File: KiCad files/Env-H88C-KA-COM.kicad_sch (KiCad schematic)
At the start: 218 parts, among them J1 TSA343G00-250J2, U1 SOT-23-5 5.5V 3.3V 500mA, U2 RP2040

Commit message: general progress
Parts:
- removed D1: 1N4002W, Diode_SMD:D_SOD-123, symbol Device:D_Schottky
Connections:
- net D+ is gone; now on net USB_D+: D18.3 (I/O2), USB1.6 (DP1), USB1.8 (DP2)
- net D- is gone; now on net USB_D-: D18.2 (I/O1), USB1.5 (DN2), USB1.7 (DN1)
- net VSYS is gone; now on net VBUS: F1.2
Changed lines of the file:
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@@
   (junction (at 342.9 43.18) (diameter 0) (color 0 0 0 0)
   )
-  (junction (at 39.37 256.54) (diameter 0) (color 0 0 0 0)
-  )
   (junction (at 241.3 43.18) (diameter 0) (color 0 0 0 0)
   )
@@
     (stroke (width 0) (type default) (color 0 0 0 0))
   )
-  (wire (pts (xy 39.37 256.54) (xy 39.37 257.81))
-    (stroke (width 0) (type default) (color 0 0 0 0))
-  )
   (wire (pts (xy 266.7 93.98) (xy 292.1 93.98))
     (stroke (width 0) (type default) (color 0 0 0 0))
@@
     (stroke (width 0) (type default) (color 0 0 0 0))
   )
-  (wire (pts (xy 30.48 256.54) (xy 39.37 256.54))
-    (stroke (width 0) (type default) (color 0 0 0 0))
-  )
   (wire (pts (xy 347.98 82.55) (xy 354.33 82.55))
     (stroke (width 0) (type default) (color 0 0 0 0))
@@
     (stroke (width 0) (type default) (color 0 0 0 0))
   )
-  (wire (pts (xy 39.37 256.54) (xy 41.91 256.54))
+  (wire (pts (xy 30.48 256.54) (xy 49.53 256.54))
     (stroke (width 0) (type default) (color 0 0 0 0))
   )
@@
     (effects (font (size 1.27 1.27)) (justify right bottom))
   )
+  (label "USB_D+" (at 88.9 219.71 0)
+    (effects (font (size 1.27 1.27)) (justify left bottom))
+  )
   (label "GPIO3" (at 299.72 307.34 180)
     (effects (font (size 1.27 1.27)) (justify right bottom))
@@
     (effects (font (size 1.27 1.27)) (justify left bottom))
   )
+  (label "USB_D-" (at 88.9 191.77 0)
+    (effects (font (size 1.27 1.27)) (justify left bottom))
+  )
   (label "GPIO19" (at 299.72 347.98 180)
     (effects (font (size 1.27 1.27)) (justify right bottom))
@@
     )
   )
-  (global_label "D-" (shape input) (at 88.9 191.77 0) (fields_autoplaced)
-    (effects (font (size 1.27 1.27)) (justify left))
-    (property "Intersheet References" "${INTERSHEET_REFS}" (id 0) (at 94.1555 191.6906 0)
-      (effects (font (size 1.27 1.27)) (justify left) hide)
-    )
-  )
   (global_label "lock2" (shape input) (at 551.18 336.55 180) (fields_autoplaced)
     (effects (font (size 1.27 1.27)) (justify right))
@@
     )
   )
-  (global_label "D+" (shape input) (at 88.9 219.71 0) (fields_autoplaced)
-    (effects (font (size 1.27 1.27)) (justify left))
-    (property "Intersheet References" "${INTERSHEET_REFS}" (id 0) (at 94.1555 219.6306 0)
-      (effects (font (size 1.27 1.27)) (justify left) hide)
-    )
-  )
   (global_label "VSYS" (shape input) (at 55.88 256.54 180) (fields_autoplaced)
     (effects (font (size 0.508 0.508)) (justify right))
@@
     (pin "2")
   )
-  (symbol (lib_id "Device:D_Schottky") (at 45.72 256.54 180) (unit 1)
-    (in_bom yes) (on_board yes)
-    (property "Reference" "D1" (id 0) (at 45.72 251.0282 0))
-    (property "Value" "1N4002W" (id 1) (at 45.72 253.3396 0))
-    (property "Footprint" "Diode_SMD:D_SOD-123" (id 2) (at 45.72 256.54 0)
-      (effects (font (size 1.27 1.27)) hide)
-    )
-    (property "Datasheet" "" (id 3) (at 45.72 256.54 0)
-      (effects (font (size 1.27 1.27)) hide)
-    )
-    (property "LCSC" " " (id 4) (at 45.72 256.54 0)
-      (effects (font (size 1.27 1.27)) hide)
-    )
-    (pin "1")
-    (pin "2")
-  )
   (symbol (lib_id "MX_Alps_Hybrid:MX-NoLED") (at 191.77 33.02 0) (unit 1)
     (in_bom yes) (on_board yes)
@@
       (reference "CBP1") (unit 1) (value "10uf 0402") (footprint "Capacitor_SMD:C_0402_1005Metric")
     )
-    (path "/8ad5387f-3794-4c4f-b55f-a5df62f92cbd"
-      (reference "D1") (unit 1) (value "1N4002W") (footprint "Diode_SMD:D_SOD-123")
-    )
     (path "/4b543e59-5223-4ac5-868a-176e1cc9c1ca"

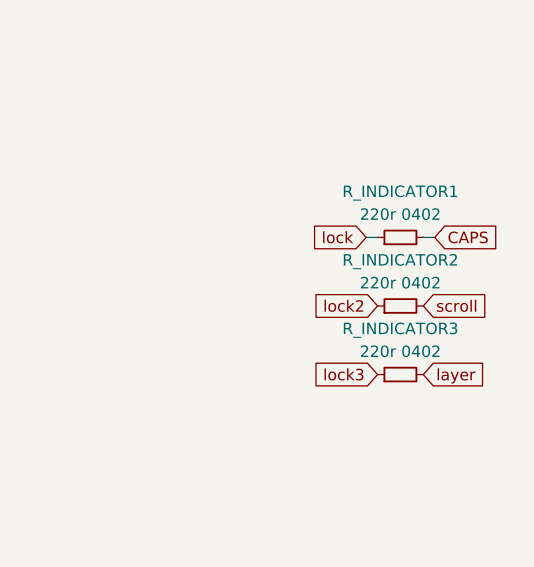
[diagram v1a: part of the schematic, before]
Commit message: slight rework to F12 TKL
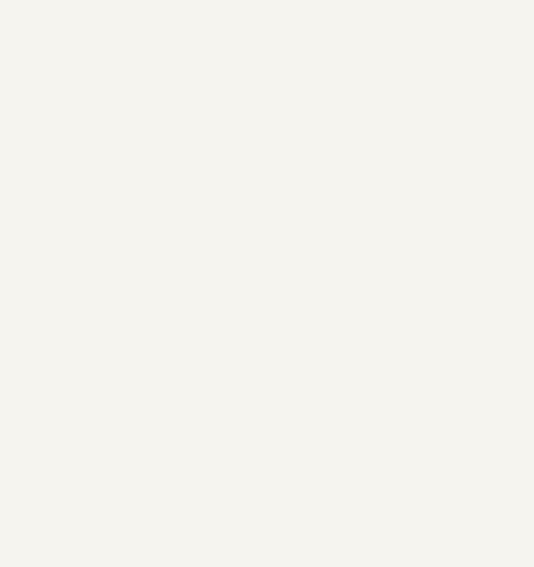
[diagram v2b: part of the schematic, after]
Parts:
- removed R_INDICATOR1, R_INDICATOR2, R_INDICATOR3: 220r 0402, Resistor_SMD:R_0402_1005Metric, symbol Device:R_Small
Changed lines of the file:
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@@
     (stroke (width 0) (type default) (color 0 0 0 0))
   )
-  (wire (pts (xy 549.91 328.93) (xy 551.18 328.93))
-    (stroke (width 0) (type solid) (color 0 0 0 0))
-  )
-  (wire (pts (xy 556.26 328.93) (xy 557.53 328.93))
-    (stroke (width 0) (type solid) (color 0 0 0 0))
-  )
   (wire (pts (xy 317.5 87.63) (xy 317.5 88.9))
     (stroke (width 0) (type default) (color 0 0 0 0))
@@
     )
   )
-  (global_label "lock3" (shape input) (at 551.18 344.17 180) (fields_autoplaced)
-    (effects (font (size 1.27 1.27)) (justify right))
-    (property "Intersheet References" "${INTERSHEET_REFS}" (id 0) (at 543.6264 344.0906 0)
-      (effects (font (size 1.27 1.27)) (justify right) hide)
-    )
-  )
   (global_label "col2" (shape input) (at 100.33 24.13 180) (fields_autoplaced)
     (effects (font (size 1.27 1.27)) (justify right))
@@
     )
   )
-  (global_label "lock2" (shape input) (at 551.18 336.55 180) (fields_autoplaced)
-    (effects (font (size 1.27 1.27)) (justify right))
-    (property "Intersheet References" "${INTERSHEET_REFS}" (id 0) (at 543.6264 336.4706 0)
-      (effects (font (size 1.27 1.27)) (justify right) hide)
-    )
-  )
   (global_label "col5" (shape input) (at 176.53 24.13 180) (fields_autoplaced)
     (effects (font (size 1.27 1.27)) (justify right))
@@
     )
   )
-  (global_label "layer" (shape input) (at 556.26 344.17 0) (fields_autoplaced)
-    (effects (font (size 1.27 1.27)) (justify left))
-    (property "Intersheet References" "${INTERSHEET_REFS}" (id 0) (at 563.3298 344.2494 0)
-      (effects (font (size 1.27 1.27)) (justify left) hide)
-    )
-  )
   (global_label "VBUS" (shape input) (at 54.61 266.7 180) (fields_autoplaced)
     (effects (font (size 1.1938 1.1938)) (justify right))
@@
     )
   )
-  (global_label "CAPS" (shape input) (at 557.53 328.93 0) (fields_autoplaced)
-    (effects (font (size 1.27 1.27)) (justify left))
-    (property "Intersheet References" "${INTERSHEET_REFS}" (id 0) (at 564.7812 329.0094 0)
-      (effects (font (size 1.27 1.27)) (justify left) hide)
-    )
-  )
   (global_label "col17" (shape input) (at 481.33 24.13 180) (fields_autoplaced)
     (effects (font (size 1.27 1.27)) (justify right))
@@
     )
   )
-  (global_label "scroll" (shape input) (at 556.26 336.55 0) (fields_autoplaced)
-    (effects (font (size 1.27 1.27)) (justify left))
-    (property "Intersheet References" "${INTERSHEET_REFS}" (id 0) (at 564.0555 336.6294 0)
-      (effects (font (size 1.27 1.27)) (justify left) hide)
-    )
-  )
   (global_label "col9" (shape input) (at 278.13 24.13 180) (fields_autoplaced)
     (effects (font (size 1.27 1.27)) (justify right))
@@
     )
   )
-  (global_label "lock" (shape input) (at 549.91 328.93 180) (fields_autoplaced)
-    (effects (font (size 1.27 1.27)) (justify right))
-    (property "Intersheet References" "${INTERSHEET_REFS}" (id 0) (at 543.5659 328.8506 0)
-      (effects (font (size 1.27 1.27)) (justify right) hide)
-    )
-  )
   (symbol (lib_id "MX_Alps_Hybrid:MX-NoLED") (at 369.57 83.82 0) (unit 1)
     (in_bom yes) (on_board yes)
@@
     (pin "2")
   )
-  (symbol (lib_id "Device:R_Small") (at 553.72 344.17 90) (unit 1)
-    (in_bom yes) (on_board yes) (fields_autoplaced)
-    (property "Reference" "R_INDICATOR3" (id 0) (at 553.72 339.09 90))
-    (property "Value" "220r 0402" (id 1) (at 553.72 341.63 90))
-    (property "Footprint" "Resistor_SMD:R_0402_1005Metric" (id 2) (at 553.72 344.17 0)
-      (effects (font (size 1.27 1.27)) hide)
-    )
-    (property "Datasheet" "~" (id 3) (at 553.72 344.17 0)
-      (effects (font (size 1.27 1.27)) hide)
-    )
-    (pin "1")
-    (pin "2")
-  )
   (symbol (lib_id "Device:C") (at 121.92 260.35 0) (unit 1)
     (in_bom yes) (on_board yes)
@@
     (pin "2")
   )
-  (symbol (lib_id "Device:R_Small") (at 553.72 336.55 90) (unit 1)
-    (in_bom yes) (on_board yes) (fields_autoplaced)
-    (property "Reference" "R_INDICATOR2" (id 0) (at 553.72 331.47 90))
-    (property "Value" "220r 0402" (id 1) (at 553.72 334.01 90))
-    (property "Footprint" "Resistor_SMD:R_0402_1005Metric" (id 2) (at 553.72 336.55 0)
-      (effects (font (size 1.27 1.27)) hide)
-    )
-    (property "Datasheet" "~" (id 3) (at 553.72 336.55 0)
-      (effects (font (size 1.27 1.27)) hide)
-    )
-    (pin "1")
-    (pin "2")
-  )
   (symbol (lib_id "power:VBUS") (at 60.96 217.17 270) (unit 1)
     (in_bom yes) (on_board yes) (fields_autoplaced)
@@
     (pin "2")
   )
-  (symbol (lib_id "Device:R_Small") (at 553.72 328.93 90) (unit 1)
-    (in_bom yes) (on_board yes) (fields_autoplaced)
-    (property "Reference" "R_INDICATOR1" (id 0) (at 553.72 323.85 90))
-    (property "Value" "220r 0402" (id 1) (at 553.72 326.39 90))
-    (property "Footprint" "Resistor_SMD:R_0402_1005Metric" (id 2) (at 553.72 328.93 0)
-      (effects (font (size 1.27 1.27)) hide)
-    )
-    (property "Datasheet" "~" (id 3) (at 553.72 328.93 0)
-      (effects (font (size 1.27 1.27)) hide)
-    )
-    (pin "1")
-    (pin "2")
-  )
   (symbol (lib_id "MX_Alps_Hybrid:MX-NoLED") (at 293.37 83.82 0) (unit 1)
     (in_bom yes) (on_board yes)
@@
       (reference "R9") (unit 1) (value "1K 0402") (footprint "Resistor_SMD:R_0402_1005Metric")
     )
-    (path "/fa70715c-66dc-4e57-b5c2-f606de39a0fb"
-      (reference "R_INDICATOR1") (unit 1) (value "220r 0402") (footprint "Resistor_SMD:R_0402_1005Metric")
-    )
-    (path "/2fea6356-43e2-441b-9841-a99d56d9f9f8"
-      (reference "R_INDICATOR2") (unit 1) (value "220r 0402") (footprint "Resistor_SMD:R_0402_1005Metric")
-    )
-    (path "/2e072b3e-37b7-4b94-b6f6-cdefcd47b73b"
-      (reference "R_INDICATOR3") (unit 1) (value "220r 0402") (footprint "Resistor_SMD:R_0402_1005Metric")
-    )
     (path "/45bdeb29-aa47-44a2-9fec-a1059b0e8c62"
